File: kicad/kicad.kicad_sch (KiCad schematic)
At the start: 76 parts, among them J1 USB_C_Receptacle_USB2.0_14P, J3 Conn_01x04_Pin, SW1 SW_Push, SW10 SW_Push, SW11 SW_Push, SW12 SW_Push, SW13 SW_Push, SW14 SW_Push, SW15 SW_Push, SW16 SW_Push, SW17 SW_Push, SW18 SW_Push, SW19 SW_Push, SW2 SW_Push, SW20 SW_Push, SW21 SW_Push, SW22 SW_Push, SW23 SW_Push, SW24 SW_Push, SW25 SW_Push, SW26 SW_Push, SW27 SW_Push, SW28 SW_Push, SW29 SW_Push, SW3 SW_Push, SW30 SW_Push, SW31 SW_Push, SW32 SW_Push, SW33 SW_Push, SW34 SW_Push, SW35 SW_Push, SW4 SW_Push, SW5 SW_Push, SW6 SW_Push, SW7 SW_Push, SW8 SW_Push, SW9 SW_Push, U1 AVR32DU32x-xPT

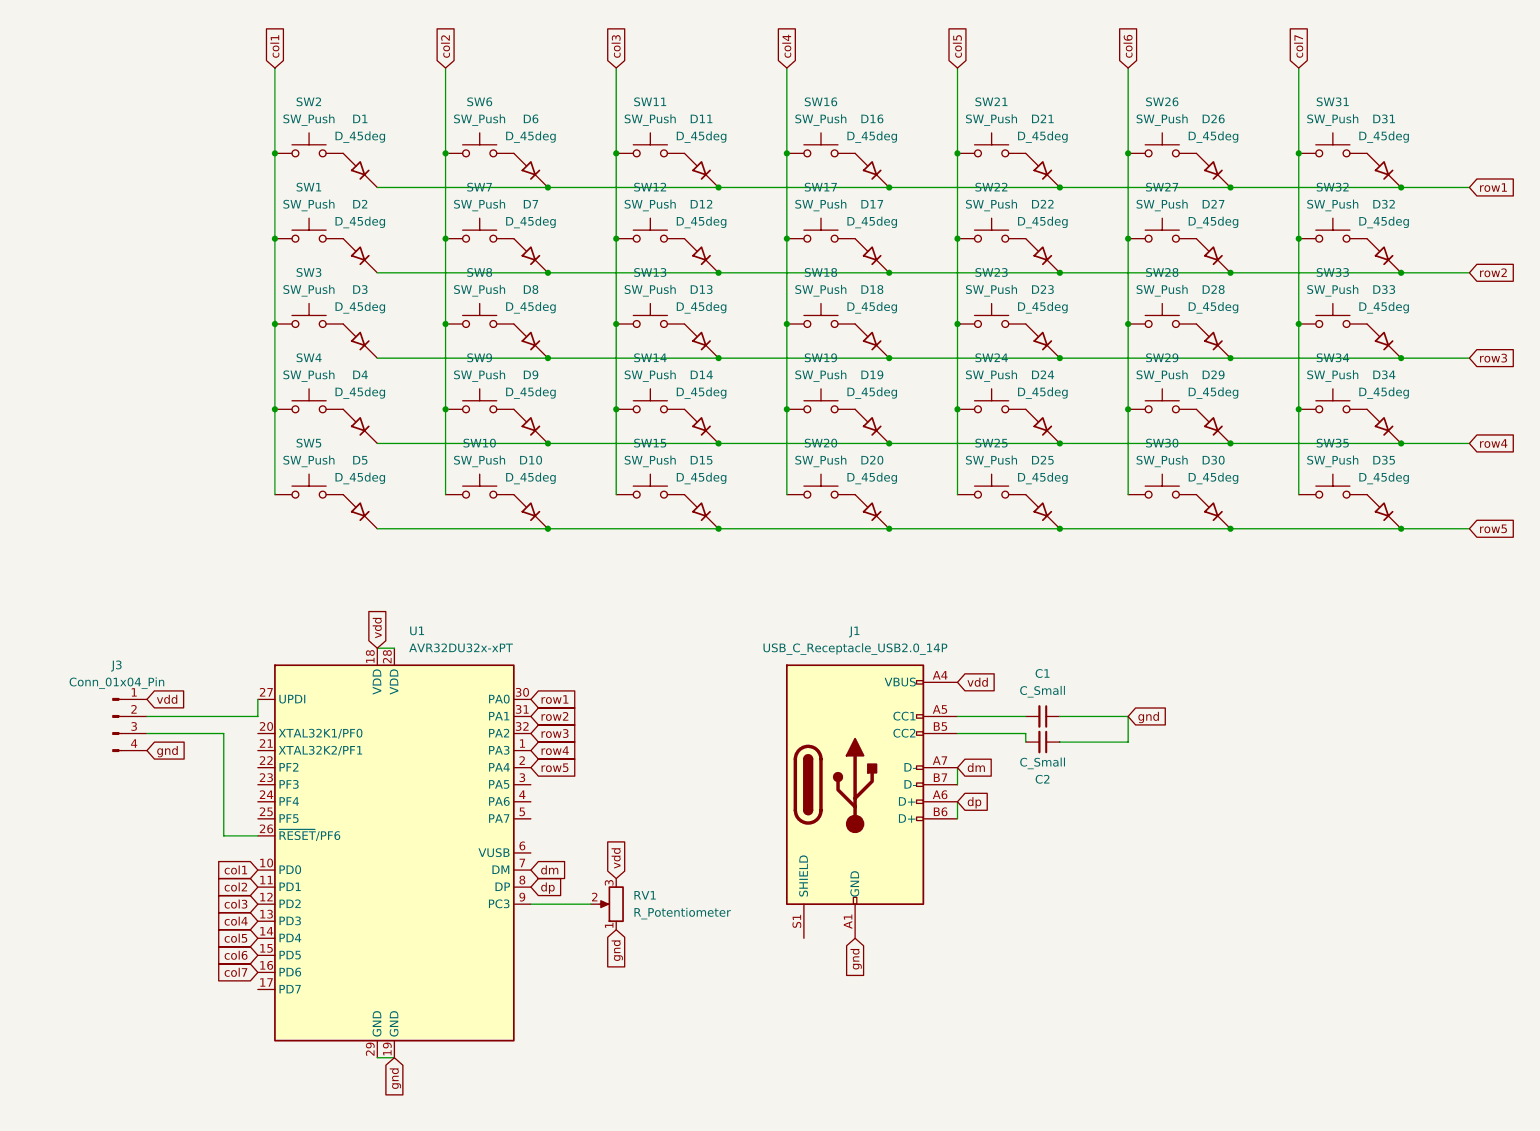
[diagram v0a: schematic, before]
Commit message: added AVR32DU32 datasheet and continued work on schematic and started work on pcb
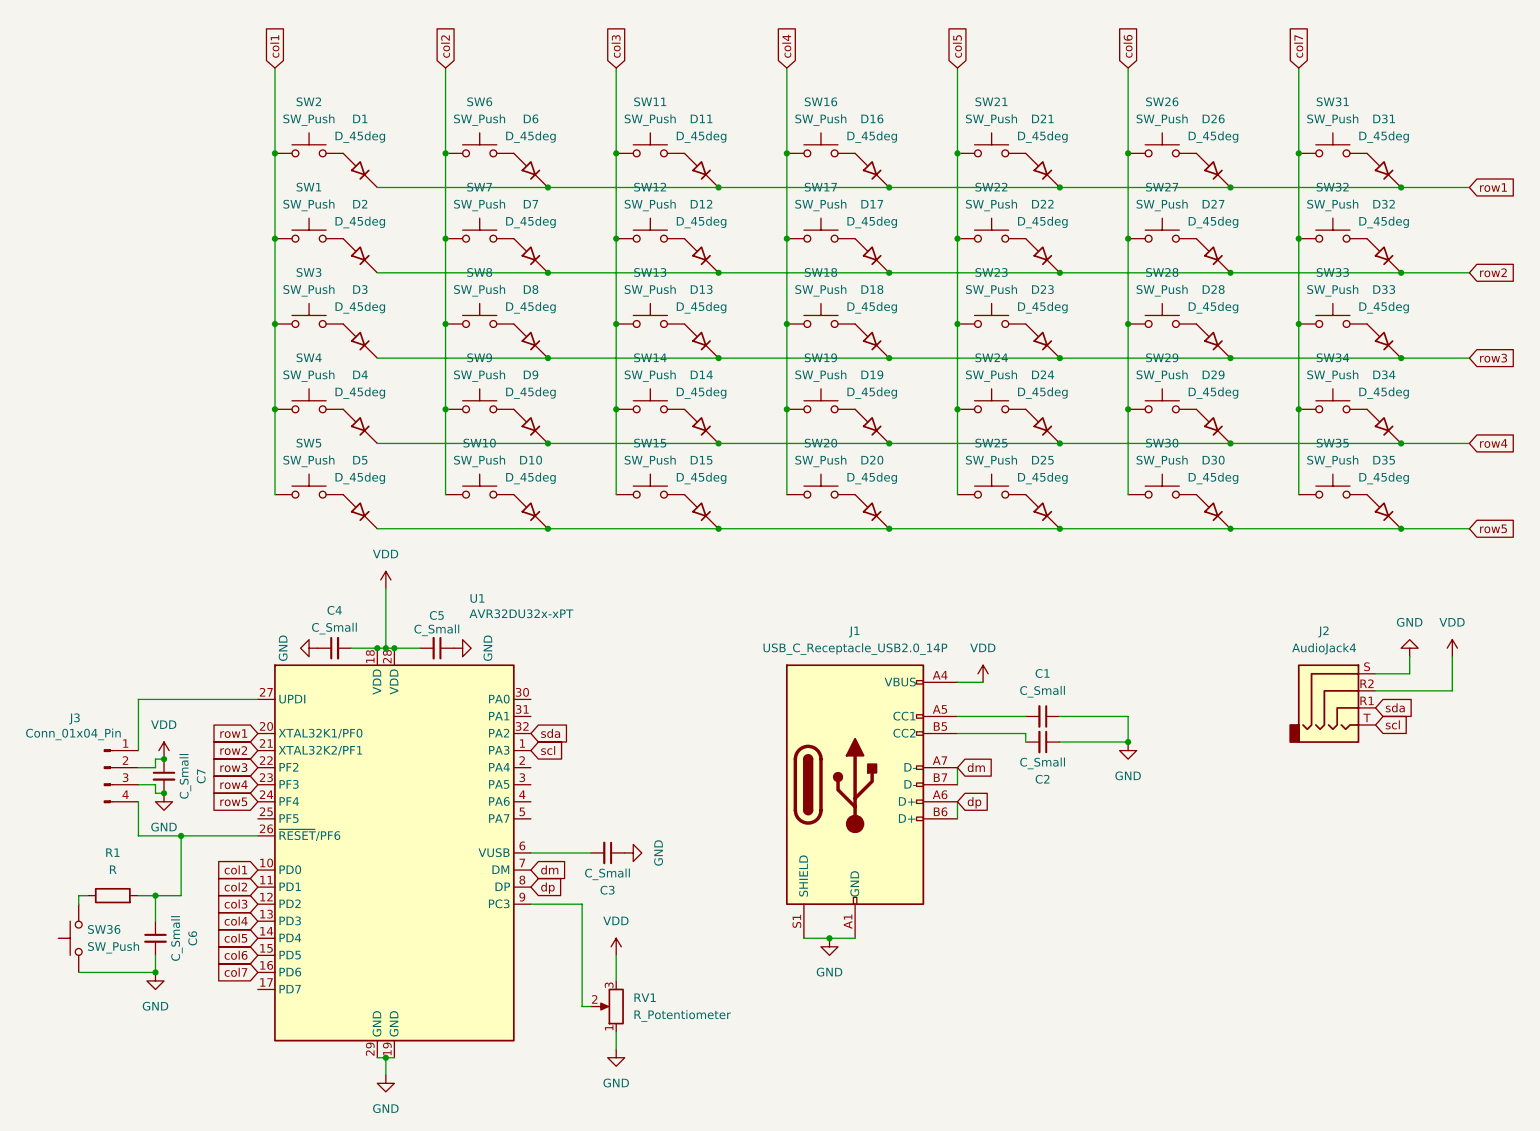
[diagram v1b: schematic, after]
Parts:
- added C3, C4, C5, C6, C7: C_Small, Capacitor_THT:C_Axial_L3.8mm_D2.6mm_P7.50mm_Horizontal, symbol Device:C_Small
- added J2: AudioJack4, Connector_Audio:Jack_3.5mm_CUI_SJ-3524-SMT_Horizontal, symbol Connector_Audio:AudioJack4
- added R1: R, Resistor_THT:R_Axial_DIN0204_L3.6mm_D1.6mm_P5.08mm_Horizontal, symbol Device:R
- added SW36: SW_Push, Button_Switch_SMD:SW_Tactile_SPST_NO_Straight_CK_PTS636Sx25SMTRLFS, symbol Switch:SW_Push
- C1, C2: footprint (none) -> Capacitor_THT:C_Axial_L3.8mm_D2.6mm_P7.50mm_Horizontal
- J1: footprint (none) -> Connector_USB:USB_C_Receptacle_Molex_105450-0101
- J3: footprint (none) -> Connector:FanPinHeader_1x04_P2.54mm_Vertical
- RV1: footprint (none) -> Potentiometer_THT:Potentiometer_ACP_CA9-V10_Vertical_Hole
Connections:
- net row1: now also U1.20 (XTAL32K1/PF0); no longer U1.30 (PA0)
- net row2: now also U1.21 (XTAL32K2/PF1); no longer U1.31 (PA1)
- net row3: now also U1.22 (PF2); no longer U1.32 (PA2)
- net row4: now also U1.23 (PF3); no longer U1.1 (PA3)
- net row5: now also U1.24 (PF4); no longer U1.2 (PA4)
- net at U1.27 (UPDI): now also J3.1 (Pin_1); no longer J3.2 (Pin_2)
- net at U1.26 (~{RESET}/PF6): now also J3.4 (Pin_4), C6.1, R1.2; no longer J3.3 (Pin_3)
- net GND: now reaches J1.S1 (SHIELD)
- net GND: now also C1.1, C2.1, J1.A1 (GND), J1.A12 (GND), J1.B1 (GND), J1.B12 (GND), J3.3 (Pin_3), RV1.1, U1.19 (GND), U1.29 (GND), C3.1, C4.1, C5.1, C6.2, C7.2, J2.S, SW36.1
- net at U1.6 (VUSB): now also C3.2
- removed net gnd: C1.1, C2.1, J1.A1 (GND), J1.A12 (GND), J1.B1 (GND), J1.B12 (GND), J3.4 (Pin_4), RV1.1, U1.19 (GND), U1.29 (GND)
- net vdd renamed VDD
- net VDD: now also J3.2 (Pin_2), C4.2, C5.2, C7.1, J2.R2; no longer J3.1 (Pin_1)
- new net: R1.1, SW36.2
- new net scl: J2.T, U1.1 (PA3)
- new net sda: J2.R1, U1.32 (PA2)
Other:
- moved on the sheet: J3, RV1
